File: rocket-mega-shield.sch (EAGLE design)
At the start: 57 parts

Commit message: working on cleaning up the shield, will have to switch to the BMP180, went through the manifest and bill of materials
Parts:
- added R1: 620k, adafruit:R-US_R1206
- added R2: 110k, adafruit:R-US_R1206
- C13: value 10nF -> 0.01uF
- C2: device adafruit:C-USC1206 -> adafruit:C-USC1210
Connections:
- new net MEGAA7: MEGA.A7, R1.1, R2.2
- net GND: now also R2.1
- net VIN: now also R1.2
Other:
- note added: "Batt Voltage"
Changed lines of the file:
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@@
 <class number="1" name="pwr" width="0.3048" drill="0">
 </class>
-<class number="2" name="raw" width="0.6096" drill="0">
+<class number="2" name="raw" width="0.3048" drill="0">
 </class>
 </classes>
@@
 <part name="GND5" library="supply1" deviceset="GND" device=""/>
 <part name="GND6" library="supply1" deviceset="GND" device=""/>
-<part name="C2" library="adafruit" deviceset="C-US" device="C1206" value="100uF16V"/>
+<part name="C2" library="adafruit" deviceset="C-US" device="C1210" value="100uF16V"/>
 <part name="C3" library="adafruit" deviceset="C-US" device="C1206" value="10uF"/>
 <part name="GND9" library="supply1" deviceset="GND" device=""/>
@@
 <part name="GND26" library="supply1" deviceset="GND" device=""/>
 <part name="C12" library="adafruit" deviceset="C-US" device="C1206" value="0.22uF"/>
-<part name="C13" library="adafruit" deviceset="C-US" device="C1206" value="10nF"/>
+<part name="C13" library="adafruit" deviceset="C-US" device="C1206" value="0.01uF"/>
 <part name="GND27" library="supply1" deviceset="GND" device=""/>
 <part name="C14" library="adafruit" deviceset="C-US" device="C1206" value="10uF"/>
@@
 <part name="RA6" library="zortness" deviceset="RESISTOR_CRA06S08" device="" value="10k"/>
 <part name="GND41" library="supply1" deviceset="GND" device=""/>
+<part name="R1" library="adafruit" deviceset="R-US_" device="R1206" value="620k"/>
+<part name="R2" library="adafruit" deviceset="R-US_" device="R1206" value="110k"/>
+<part name="GND13" library="supply1" deviceset="GND" device=""/>
 </parts>
 <sheets>
 <sheet>
 <plain>
-<wire x1="-152.4" y1="114.3" x2="-152.4" y2="73.66" width="0.1524" layer="97"/>
-<wire x1="-152.4" y1="73.66" x2="-35.56" y2="73.66" width="0.1524" layer="97"/>
-<wire x1="-35.56" y1="73.66" x2="-35.56" y2="114.3" width="0.1524" layer="97"/>
+<wire x1="-152.4" y1="114.3" x2="-152.4" y2="71.12" width="0.1524" layer="97"/>
+<wire x1="-152.4" y1="71.12" x2="-35.56" y2="71.12" width="0.1524" layer="97"/>
+<wire x1="-35.56" y1="71.12" x2="-35.56" y2="114.3" width="0.1524" layer="97"/>
 <wire x1="-35.56" y1="114.3" x2="-152.4" y2="114.3" width="0.1524" layer="97"/>
 <text x="-149.86" y="111.76" size="1.778" layer="97">Power Source Mgmt</text>
@@
 <wire x1="-147.32" y1="25.4" x2="-162.56" y2="25.4" width="0.1524" layer="97"/>
 <text x="-162.052" y="26.162" size="1.778" layer="97">Continuity</text>
+<text x="-162.56" y="17.78" size="1.778" layer="97">Batt Voltage</text>
 </plain>
 <instances>
@@
 <instance part="RA6" gate="G$1" x="78.74" y="-25.4"/>
 <instance part="GND41" gate="1" x="91.44" y="-40.64"/>
+<instance part="R1" gate="G$1" x="-88.9" y="83.82"/>
+<instance part="R2" gate="G$1" x="-106.68" y="83.82"/>
+<instance part="GND13" gate="1" x="-114.3" y="83.82" rot="R270"/>
 </instances>
 <busses>
@@
 <pinref part="GND41" gate="1" pin="GND"/>
 </segment>
+<segment>
+<pinref part="R2" gate="G$1" pin="1"/>
+<pinref part="GND13" gate="1" pin="GND"/>
+</segment>
 </net>
 <net name="VCC3" class="1">
@@
 <segment>
 <pinref part="D1" gate="G$1" pin="C"/>
-<label x="-100.33" y="88.9" size="1.778" layer="95"/>
+<label x="-105.41" y="88.9" size="1.778" layer="95"/>
 <pinref part="C2" gate="G$1" pin="1"/>
-<wire x1="-121.92" y1="91.44" x2="-76.2" y2="91.44" width="0.1524" layer="91"/>
+<wire x1="-121.92" y1="91.44" x2="-83.82" y2="91.44" width="0.1524" layer="91"/>
+<wire x1="-83.82" y1="91.44" x2="-76.2" y2="91.44" width="0.1524" layer="91"/>
 <wire x1="-76.2" y1="91.44" x2="-63.5" y2="91.44" width="0.1524" layer="91"/>
 <junction x="-76.2" y="91.44"/>
 <pinref part="3.3VREG" gate="G$1" pin="IN"/>
+<wire x1="-83.82" y1="91.44" x2="-83.82" y2="83.82" width="0.1524" layer="91"/>
+<junction x="-83.82" y="91.44"/>
+<pinref part="R1" gate="G$1" pin="2"/>
 </segment>
 </net>
@@
 </segment>
 </net>
+<net name="MEGAA7" class="0">
+<segment>
+<pinref part="MEGA" gate="G$1" pin="A7"/>
+<wire x1="-124.46" y1="17.78" x2="-144.78" y2="17.78" width="0.1524" layer="91"/>
+<label x="-144.78" y="17.78" size="1.778" layer="95"/>
+</segment>
+<segment>
+<pinref part="R2" gate="G$1" pin="2"/>
+<pinref part="R1" gate="G$1" pin="1"/>
+<wire x1="-101.6" y1="83.82" x2="-99.06" y2="83.82" width="0.1524" layer="91"/>
+<wire x1="-99.06" y1="83.82" x2="-93.98" y2="83.82" width="0.1524" layer="91"/>
+<wire x1="-99.06" y1="83.82" x2="-99.06" y2="76.2" width="0.1524" layer="91"/>
+<junction x="-99.06" y="83.82"/>
+<label x="-99.06" y="73.66" size="1.778" layer="95" rot="R90"/>
+</segment>
+</net>

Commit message: changed sd card, added holes to die down xb, changed reset switch, renamed all parts to match conventions, various other cleanup, adjusted BOM and manifest
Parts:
- removed ALTIMETER: BMP085, kurt:BMP085
- removed MICROSD: MICROSD, adafruit:MICROSD
- removed RESET: 1101NE, SparkFun-Electromechanical:SWITCH-MOMENTARY-2-SMD-1101NE
- added J2: MICROSD, zortness:MICROSD
- added S2: KMR2, zortness:TAC_SWITCHKMR2
- added U1: BMP180, zortness:BMP180
- D2: value (none) -> PWR - green
- D3: value (none) -> SDAct - orange
- D4: value (none) -> RSSI - yellow
- D5: value (none) -> Fix - blue
- D6: value (none) -> Pyro1 - red
- D7: value (none) -> Pyro2 - red
- D8: value (none) -> Pyro3 - red
- D9: value (none) -> Pyro4 - red
- J1: value (none) -> ExtBatt
- J3: value ARDUINO-MEGAFULL -> Mega R3
- renumbered 16GACCEL to U6, 200GACCEL to U8, 3.3VREG to U3, CONV to U9, E1 to D6, E2 to D7, E3 to D8, E4 to D9, EXTBATT to J1, FIRST to Q3, FIX to D5, FOURTH to Q6, GPS to U2, GYRO to U7, MEGA to J3, PWR to D2, PYRO to J4, RSSI to D4, SCLSHIFT to Q2, SDACT to D3, SDASHIFT to Q1, SECOND to Q4, THIRD to Q5, XBEE to J5, XBEESELECT to S1
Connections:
- net GND: now also J2.CARD_DETECT, J2.CARD_DETECT1, J2.GND, J2.GND1, J2.VSS, S2.3, S2.4, U1.GND; no longer ALTIMETER.GND, MICROSD.CARD_DETECT, MICROSD.CARD_DETECT1, MICROSD.GND, MICROSD.GND1, MICROSD.VSS, RESET.2
- net MEGAMISO: now also J2.DATA_OUT; no longer MICROSD.DATA_OUT
- net MOSI: now also J2.DATA_IN; no longer MICROSD.DATA_IN
- net RESET: now also S2.1, S2.2; no longer RESET.1
- net SCL: now also U1.SCL; no longer ALTIMETER.SCL
- net SCLK: now also J2.SCLK; no longer MICROSD.SCLK
- net SDA: now also U1.SDA; no longer ALTIMETER.SDA
- net SDCS: now also J2.CS; no longer MICROSD.CS
- net VCC3: now also J2.VDD, U1.VDD, U1.VDDIO; no longer ALTIMETER.VDDA, ALTIMETER.VDDD, MICROSD.VDD

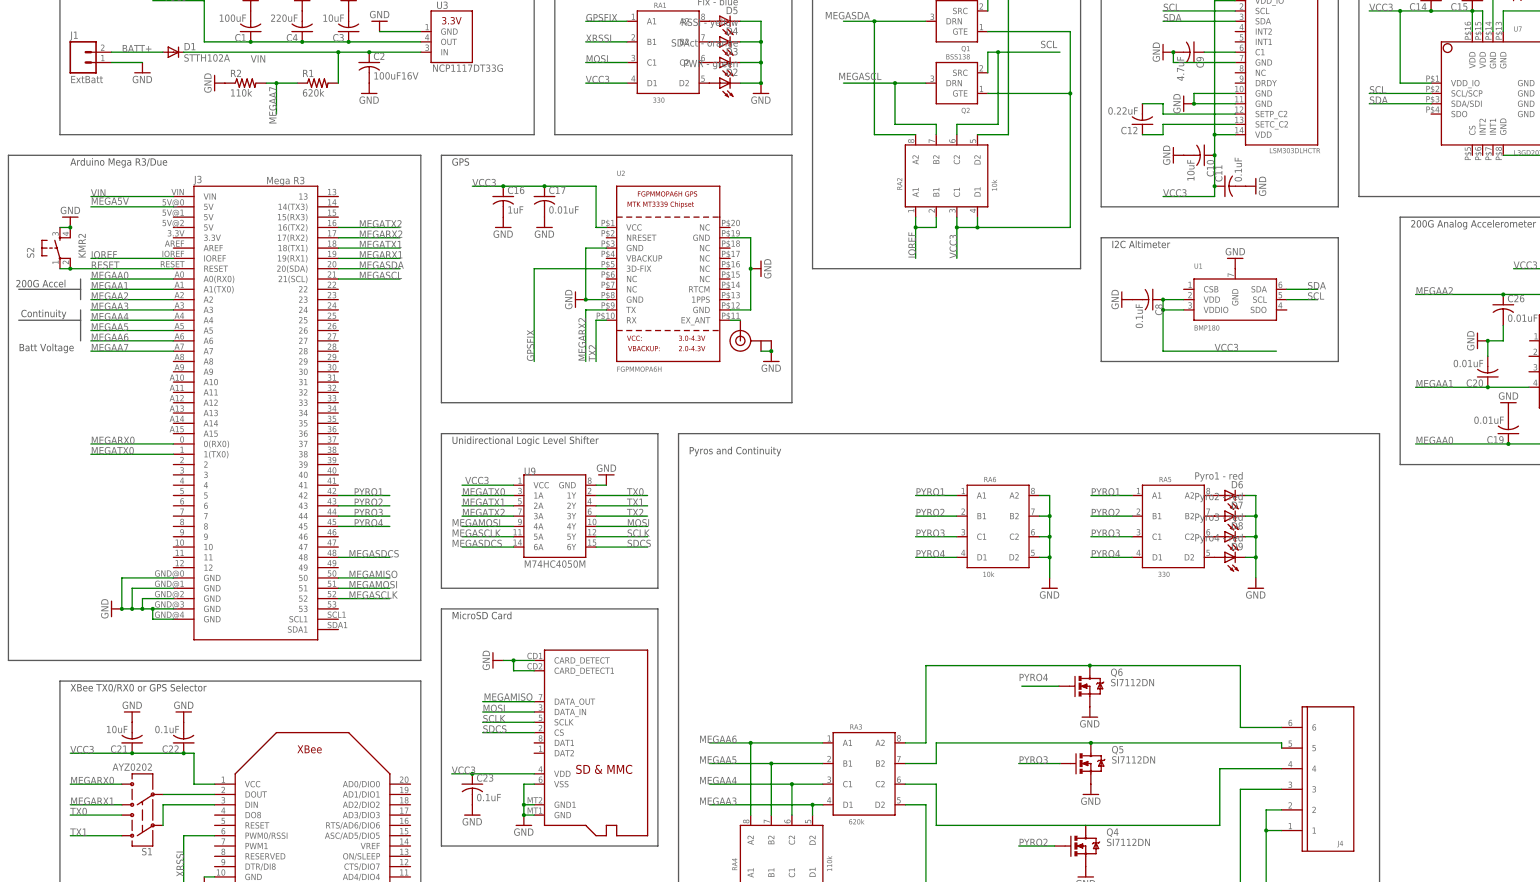
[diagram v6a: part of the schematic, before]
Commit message: added buzzer on pin 8, moved all analog reads down to second set of pins, A8-A15, updated manifest, bom, and images
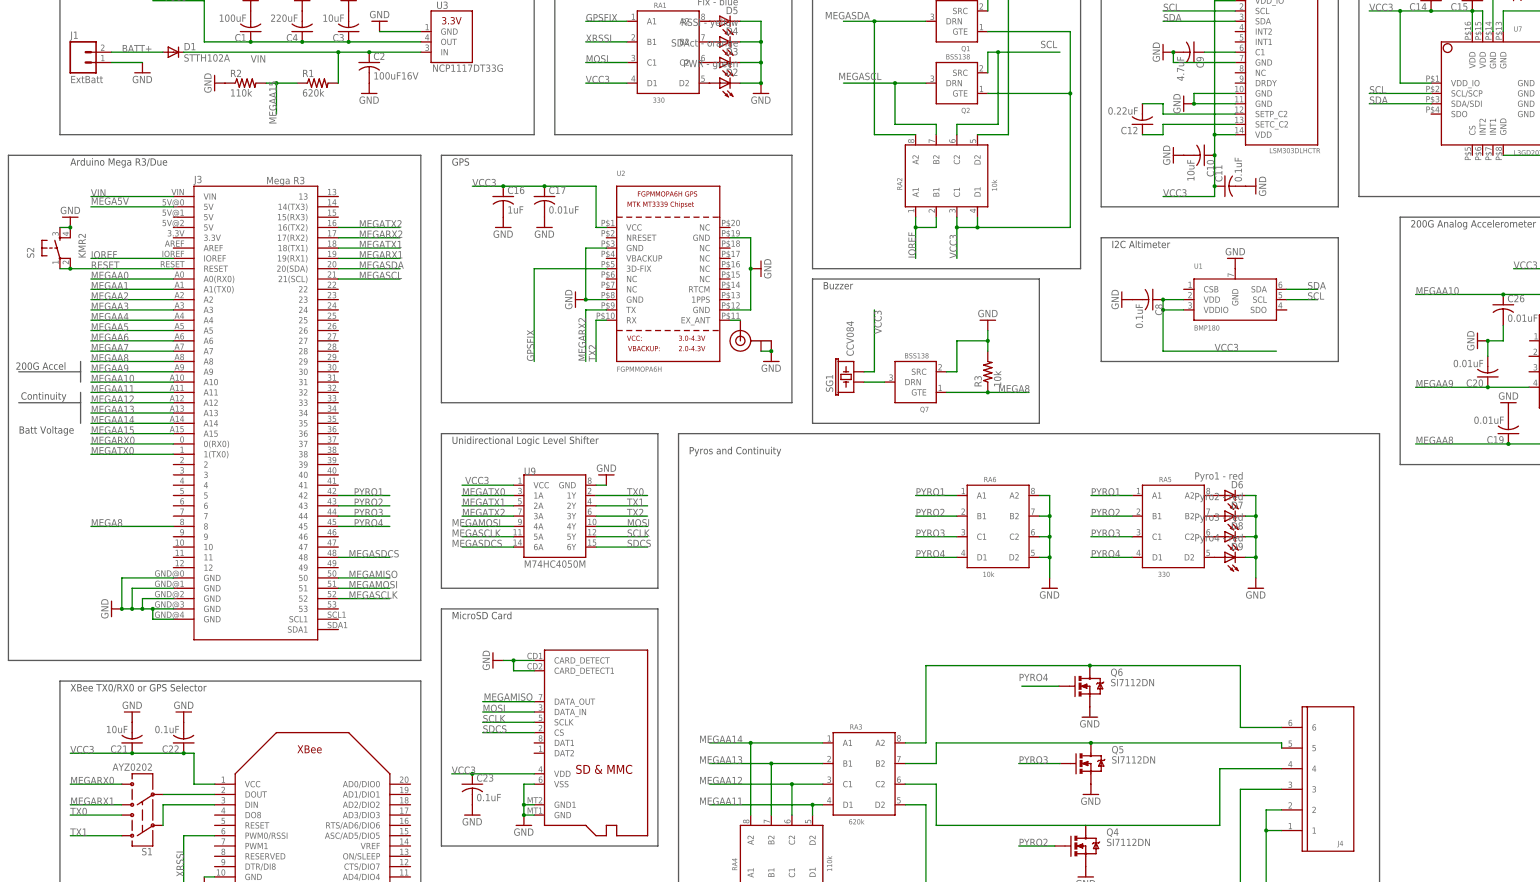
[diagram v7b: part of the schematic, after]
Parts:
- added Q7: BSS138, kurt:BSS138
- added R3: 10k, adafruit:R-US_R1206
- added SG1: CCV084, SparkFun-Electromechanical:BUZZERSMD2
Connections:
- new net MEGA8: J3.8, Q7.GTE, R3.1
- new net MEGAA10: C26.1, J3.A10, U8.Z
- new net MEGAA11: J3.A11, RA3.D1, RA4.D2
- new net MEGAA12: J3.A12, RA3.C1, RA4.C2
- new net MEGAA13: J3.A13, RA3.B1, RA4.B2
- new net MEGAA14: J3.A14, RA3.A1, RA4.A2
- new net MEGAA15: J3.A15, R1.1, R2.2
- new net MEGAA8: C19.1, J3.A8, U8.X
- new net MEGAA9: C20.1, J3.A9, U8.Y
- new net N$13: Q7.DRN, SG1.1
- net GND: now also Q7.SRC, R3.2
- net MEGAA0: no longer C19.1, U8.X
- net MEGAA1: no longer C20.1, U8.Y
- net MEGAA2: no longer C26.1, U8.Z
- net MEGAA3: no longer RA3.D1, RA4.D2
- net MEGAA4: no longer RA3.C1, RA4.C2
- net MEGAA5: no longer RA3.B1, RA4.B2
- net MEGAA6: no longer RA3.A1, RA4.A2
- net MEGAA7: no longer R1.1, R2.2
- net VCC3: now also SG1.2
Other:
- note added: "Buzzer"

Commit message: added LED on pin 13, more cleanup, updated BOM
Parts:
- added D10: 13 - red, SparkFun-LED:LED1206
- added R4: 330, adafruit:R-US_R1206
- renumbered GPS_EXT to J6
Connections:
- new net N$14: D10.A, R4.2
- new net N$9: J3.13, R4.1
- net GND: now also D10.C
- net MOSI: no longer RA1.C1
- net SCLK: now also RA1.C1
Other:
- moved on the sheet: D6, D7, D8, D9, J4, Q3, Q4, Q5, Q6, RA3, RA4, RA5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
